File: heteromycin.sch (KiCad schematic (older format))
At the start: 0 parts

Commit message: Current snapshot
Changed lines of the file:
@@
 $Descr A4 11693 8268
 encoding utf-8
-Sheet 1 7
+Sheet 1 11
 Title ""
 Date ""
@@
 $EndSheet
 $Sheet
-S 8550 1950 1600 950
+S 8550 1950 1600 600
 U 5BC2F52C
 F0 "Stepper Motor X" 50
@@
 F1 "mosfets.sch" 50
 $EndSheet
+$Sheet
+S 8550 2750 1600 600
+U 5BC77BE8
+F0 "Steper Motor Y" 50
+F1 "motor.sch" 50
+$EndSheet
+$Sheet
+S 8550 3550 1600 600
+U 5BC77F87
+F0 "Stepper Motor Z" 50
+F1 "motor.sch" 50
+$EndSheet
+$Sheet
+S 8550 4350 1600 600
+U 5BC77F8A
+F0 "Stepper Motor E0" 50
+F1 "motor.sch" 50
+$EndSheet
+$Sheet
+S 8550 5150 1600 600
+U 5BC77F8D
+F0 "Stepper Motor E1" 50
+F1 "motor.sch" 50
+$EndSheet
 $EndSCHEMATC

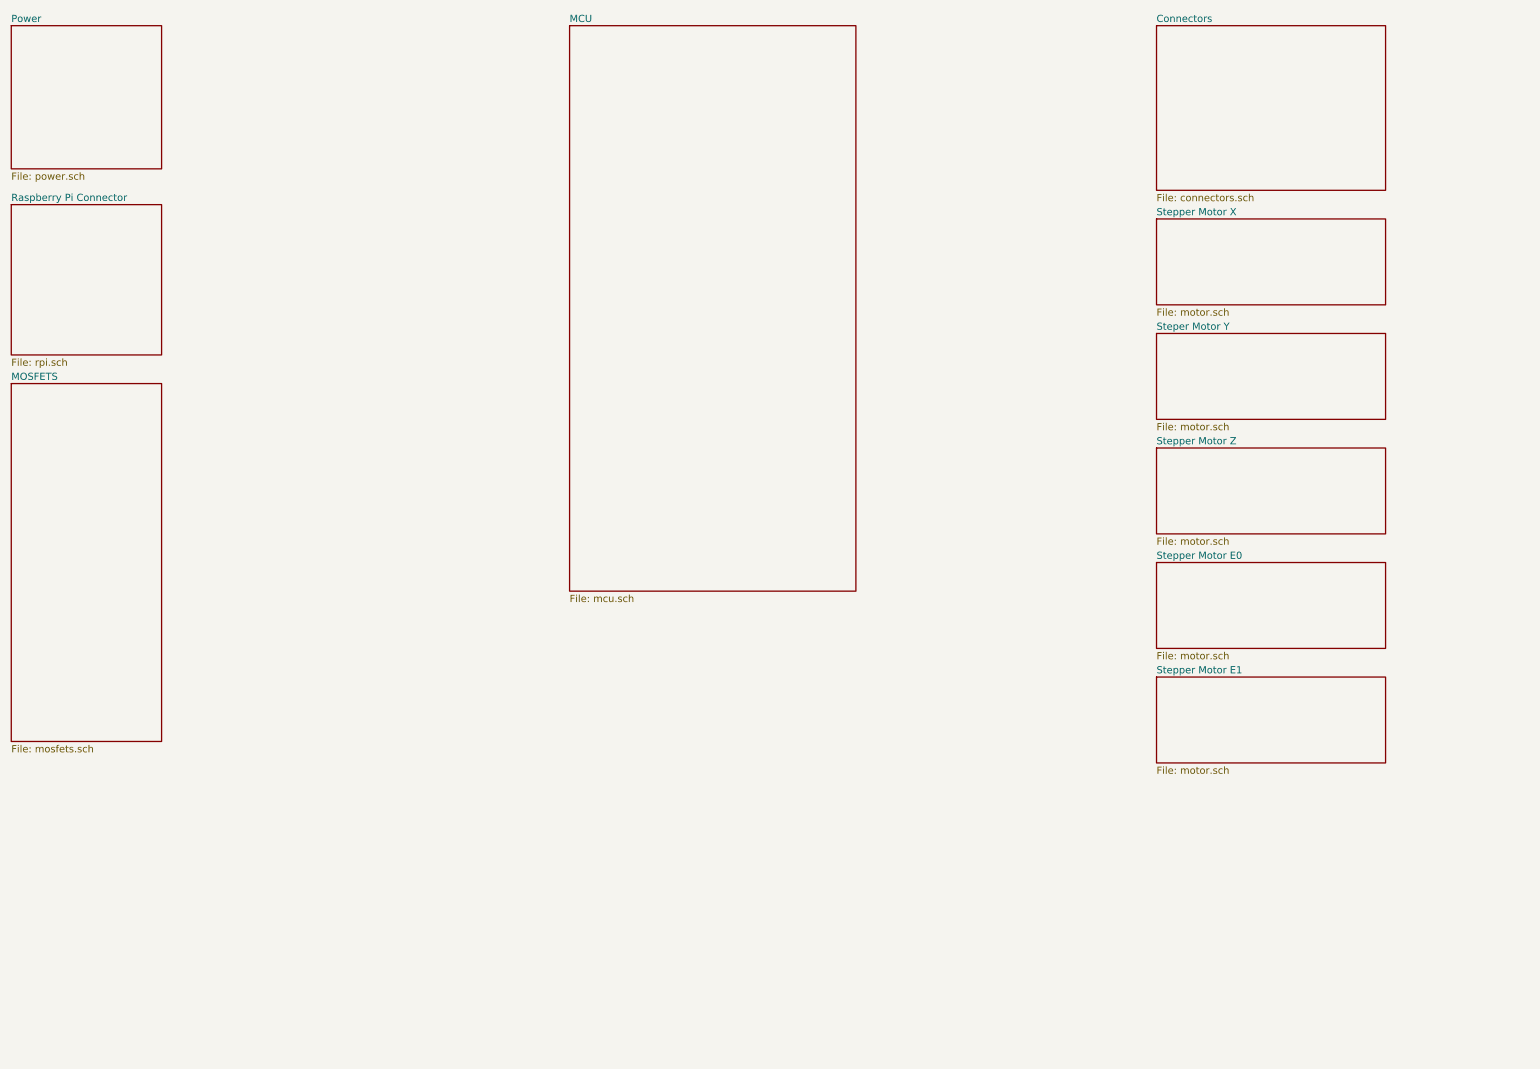
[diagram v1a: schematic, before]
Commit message: Add SD card reader, placed temp connections, fixed stepper placement
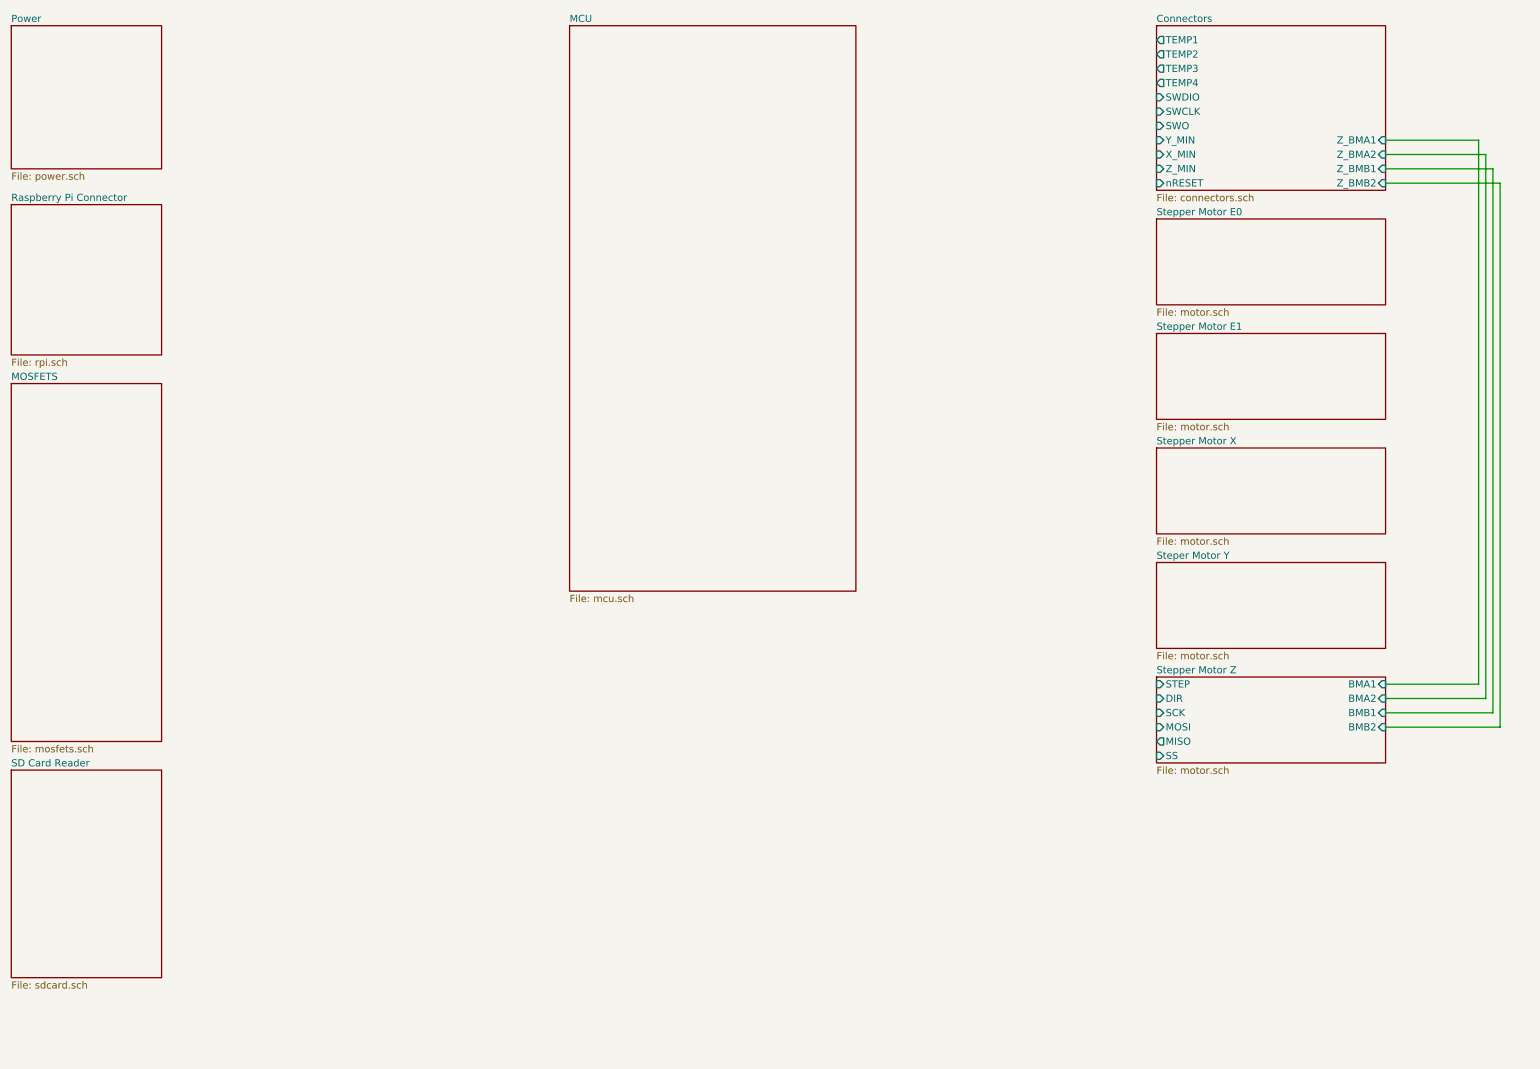
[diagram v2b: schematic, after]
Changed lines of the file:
@@
 $Descr A4 11693 8268
 encoding utf-8
-Sheet 1 11
+Sheet 1 12
 Title ""
 Date ""
@@
 F0 "Connectors" 50
 F1 "connectors.sch" 50
+F2 "TEMP1" O L 8550 700 50
+F3 "TEMP2" O L 8550 800 50
+F4 "TEMP3" O L 8550 900 50
+F5 "nRESET" I L 8550 1700 50
+F6 "SWDIO" I L 8550 1100 50
+F7 "SWCLK" I L 8550 1200 50
+F8 "Z_MIN" I L 8550 1600 50
+F9 "Y_MIN" I L 8550 1400 50
+F10 "Z_BMB1" I R 10150 1600 50
+F11 "Z_BMB2" I R 10150 1700 50
+F12 "Z_BMA2" I R 10150 1500 50
+F13 "Z_BMA1" I R 10150 1400 50
+F14 "X_MIN" I L 8550 1500 50
+F15 "SWO" I L 8550 1300 50
+F16 "TEMP4" O L 8550 1000 50
 $EndSheet
 $Sheet
-S 8550 1950 1600 600
+S 8550 3550 1600 600
 U 5BC2F52C
 F0 "Stepper Motor X" 50
@@
 $EndSheet
 $Sheet
-S 8550 2750 1600 600
+S 8550 4350 1600 600
 U 5BC77BE8
 F0 "Steper Motor Y" 50
@@
 $EndSheet
 $Sheet
-S 8550 3550 1600 600
+S 8550 5150 1600 600
 U 5BC77F87
 F0 "Stepper Motor Z" 50
 F1 "motor.sch" 50
+F2 "STEP" I L 8550 5200 50
+F3 "DIR" I L 8550 5300 50
+F4 "SCK" I L 8550 5400 50
+F5 "MOSI" I L 8550 5500 50
+F6 "MISO" O L 8550 5600 50
+F7 "BMA1" I R 10150 5200 50
+F8 "BMA2" I R 10150 5300 50
+F9 "BMB2" I R 10150 5500 50
+F10 "BMB1" I R 10150 5400 50
+F11 "SS" I L 8550 5700 50
 $EndSheet
 $Sheet
-S 8550 4350 1600 600
+S 8550 1950 1600 600
 U 5BC77F8A
 F0 "Stepper Motor E0" 50
@@
 $EndSheet
 $Sheet
-S 8550 5150 1600 600
+S 8550 2750 1600 600
 U 5BC77F8D
 F0 "Stepper Motor E1" 50
 F1 "motor.sch" 50
 $EndSheet
+Wire Wire Line
+	10150 5200 10800 5200
+Wire Wire Line
+	10800 5200 10800 1400
+Wire Wire Line
+	10800 1400 10150 1400
+Wire Wire Line
+	10150 1500 10850 1500
+Wire Wire Line
+	10850 1500 10850 5300
+Wire Wire Line
+	10850 5300 10150 5300
+Wire Wire Line
+	10150 5400 10900 5400
+Wire Wire Line
+	10900 5400 10900 1600
+Wire Wire Line
+	10900 1600 10150 1600
+Wire Wire Line
+	10150 1700 10950 1700
+Wire Wire Line
+	10950 1700 10950 5500
+Wire Wire Line
+	10950 5500 10150 5500
+$Sheet
+S 550  5800 1050 1450
+U 5BC78E83
+F0 "SD Card Reader" 50
+F1 "sdcard.sch" 50
+$EndSheet
 $EndSCHEMATC

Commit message: Some small adjustments
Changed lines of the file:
@@
 $EndDescr
 $Sheet
-S 550  1850 1050 1050
+S 550  600  1050 1050
 U 5BC4AC32
 F0 "Raspberry Pi Connector" 50
@@
 $EndSheet
 $Sheet
-S 550  600  1050 1000
+S 5700 6550 1150 1100
 U 5BC54251
 F0 "Power" 50
@@
 $EndSheet
 $Sheet
-S 4450 600  2000 3950
+S 4350 600  2000 3950
 U 5BC1C8A4
 F0 "MCU" 50
@@
 $EndSheet
 $Sheet
-S 8550 600  1600 1150
+S 550  4300 1050 650
+U 5BC2F52C
+F0 "Stepper Motor X" 50
+F1 "motor.sch" 50
+F2 "STEP" I R 1600 4350 50
+F3 "DIR" I R 1600 4450 50
+F4 "SCK" I R 1600 4550 50
+F5 "MOSI" I R 1600 4650 50
+F6 "MISO" O R 1600 4750 50
+F7 "SS" I R 1600 4850 50
+$EndSheet
+$Sheet
+S 550  1800 1050 750
+U 5BC2F648
+F0 "MOSFETS" 50
+F1 "mosfets.sch" 50
+F2 "PWM_BED" I R 1600 1850 50
+F3 "PWM_HEAT1" I R 1600 1950 50
+F4 "PWM_FAN1" I R 1600 2150 50
+F5 "PWM_FAN3" I R 1600 2350 50
+F6 "PWM_HEAT2" I R 1600 2050 50
+F7 "PWM_FAN2" I R 1600 2250 50
+F8 "PWM_FAN4" I R 1600 2450 50
+$EndSheet
+$Sheet
+S 550  5100 1050 650
+U 5BC77BE8
+F0 "Steper Motor Y" 50
+F1 "motor.sch" 50
+F2 "STEP" I R 1600 5150 50
+F3 "DIR" I R 1600 5250 50
+F4 "SCK" I R 1600 5350 50
+F5 "MOSI" I R 1600 5450 50
+F6 "MISO" O R 1600 5550 50
+F7 "SS" I R 1600 5650 50
+$EndSheet
+$Sheet
+S 550  5900 1050 1050
+U 5BC77F87
+F0 "Stepper Motor Z" 50
+F1 "motor.sch" 50
+F2 "STEP" I R 1600 5950 50
+F3 "DIR" I R 1600 6050 50
+F4 "SCK" I R 1600 6150 50
+F5 "MOSI" I R 1600 6250 50
+F6 "MISO" O R 1600 6350 50
+F7 "BMA1" I R 1600 6550 50
+F8 "BMA2" I R 1600 6650 50
+F9 "BMB2" I R 1600 6850 50
+F10 "BMB1" I R 1600 6750 50
+F11 "SS" I R 1600 6450 50
+$EndSheet
+$Sheet
+S 550  3500 1050 650
+U 5BC77F8A
+F0 "Stepper Motor E0" 50
+F1 "motor.sch" 50
+F2 "STEP" I R 1600 3550 50
+F3 "DIR" I R 1600 3650 50
+F4 "SCK" I R 1600 3750 50
+F5 "MOSI" I R 1600 3850 50
+F6 "MISO" O R 1600 3950 50
+F7 "SS" I R 1600 4050 50
+$EndSheet
+$Sheet
+S 550  2700 1050 650
+U 5BC77F8D
+F0 "Stepper Motor E1" 50
+F1 "motor.sch" 50
+F2 "STEP" I R 1600 2750 50
+F3 "DIR" I R 1600 2850 50
+F4 "SCK" I R 1600 2950 50
+F5 "MOSI" I R 1600 3050 50
+F6 "MISO" O R 1600 3150 50
+F7 "SS" I R 1600 3250 50
+$EndSheet
+$Sheet
+S 9800 600  1350 550
+U 5BC78E83
+F0 "SD Card Reader" 50
+F1 "sdcard.sch" 50
+F2 "MISO" I L 9800 850 50
+F3 "MOSI" I L 9800 750 50
+F4 "SCK" I L 9800 650 50
+F5 "SD_DETECT" I L 9800 1050 50
+F6 "SS" I L 9800 950 50
+$EndSheet
+$Sheet
+S 9800 1300 1350 4100
 U 5BC2F290
 F0 "Connectors" 50
 F1 "connectors.sch" 50
-F2 "TEMP1" O L 8550 700 50
-F3 "TEMP2" O L 8550 800 50
-F4 "TEMP3" O L 8550 900 50
-F5 "nRESET" I L 8550 1700 50
-F6 "SWDIO" I L 8550 1100 50
-F7 "SWCLK" I L 8550 1200 50
-F8 "Z_MIN" I L 8550 1600 50
-F9 "Y_MIN" I L 8550 1400 50
-F10 "Z_BMB1" I R 10150 1600 50
-F11 "Z_BMB2" I R 10150 1700 50
-F12 "Z_BMA2" I R 10150 1500 50
-F13 "Z_BMA1" I R 10150 1400 50
-F14 "X_MIN" I L 8550 1500 50
-F15 "SWO" I L 8550 1300 50
-F16 "TEMP4" O L 8550 1000 50
-$EndSheet
-$Sheet
-S 8550 3550 1600 600
-U 5BC2F52C
-F0 "Stepper Motor X" 50
-F1 "motor.sch" 50
-$EndSheet
-$Sheet
-S 550  3100 1050 2500
-U 5BC2F648
-F0 "MOSFETS" 50
-F1 "mosfets.sch" 50
-$EndSheet
-$Sheet
-S 8550 4350 1600 600
-U 5BC77BE8
-F0 "Steper Motor Y" 50
-F1 "motor.sch" 50
-$EndSheet
-$Sheet
-S 8550 5150 1600 600
-U 5BC77F87
-F0 "Stepper Motor Z" 50
-F1 "motor.sch" 50
-F2 "STEP" I L 8550 5200 50
-F3 "DIR" I L 8550 5300 50
-F4 "SCK" I L 8550 5400 50
-F5 "MOSI" I L 8550 5500 50
-F6 "MISO" O L 8550 5600 50
-F7 "BMA1" I R 10150 5200 50
-F8 "BMA2" I R 10150 5300 50
-F9 "BMB2" I R 10150 5500 50
-F10 "BMB1" I R 10150 5400 50
-F11 "SS" I L 8550 5700 50
-$EndSheet
-$Sheet
-S 8550 1950 1600 600
-U 5BC77F8A
-F0 "Stepper Motor E0" 50
-F1 "motor.sch" 50
-$EndSheet
-$Sheet
-S 8550 2750 1600 600
-U 5BC77F8D
-F0 "Stepper Motor E1" 50
-F1 "motor.sch" 50
+F2 "Z_BMB1" I L 9800 5250 50
+F3 "Z_BMB2" I L 9800 5350 50
+F4 "Z_BMA2" I L 9800 5150 50
+F5 "Z_BMA1" I L 9800 5050 50
+F6 "TEMP1" O L 9800 2550 50
+F7 "TEMP2" O L 9800 2650 50
+F8 "TEMP3" O L 9800 2850 50
+F9 "nRESET" I L 9800 3450 50
+F10 "SWDIO" I L 9800 3250 50
+F11 "SWCLK" I L 9800 3150 50
+F12 "Z_MIN" I L 9800 4000 50
+F13 "Y_MIN" I L 9800 3900 50
+F14 "X_MIN" I L 9800 3800 50
+F15 "SWO" I L 9800 3350 50
+F16 "TEMP4" O L 9800 2750 50
 $EndSheet
 Wire Wire Line
-	10150 5200 10800 5200
+	1600 6850 5550 6850
 Wire Wire Line
-	10800 5200 10800 1400
+	5550 6850 5550 6400
 Wire Wire Line
-	10800 1400 10150 1400
+	5550 6400 9600 6400
 Wire Wire Line
-	10150 1500 10850 1500
+	9600 6400 9600 5350
 Wire Wire Line
-	10850 1500 10850 5300
+	9600 5350 9800 5350
 Wire Wire Line
-	10850 5300 10150 5300
+	9800 5250 9500 5250
 Wire Wire Line
-	10150 5400 10900 5400
+	9500 5250 9500 6300
 Wire Wire Line
-	10900 5400 10900 1600
+	9500 6300 5450 6300
 Wire Wire Line
-	10900 1600 10150 1600
+	5450 6300 5450 6750
 Wire Wire Line
-	10150 1700 10950 1700
+	5450 6750 1600 6750
 Wire Wire Line
-	10950 1700 10950 5500
+	1600 6650 5350 6650
 Wire Wire Line
-	10950 5500 10150 5500
-$Sheet
-S 550  5800 1050 1450
-U 5BC78E83
-F0 "SD Card Reader" 50
-F1 "sdcard.sch" 50
-$EndSheet
+	5350 6650 5350 6200
+Wire Wire Line
+	5350 6200 9400 6200
+Wire Wire Line
+	9400 6200 9400 5150
+Wire Wire Line
+	9400 5150 9800 5150
+Wire Wire Line
+	9800 5050 9300 5050
+Wire Wire Line
+	9300 5050 9300 6100
+Wire Wire Line
+	9300 6100 5250 6100
+Wire Wire Line
+	5250 6100 5250 6550
+Wire Wire Line
+	5250 6550 1600 6550
 $EndSCHEMATC

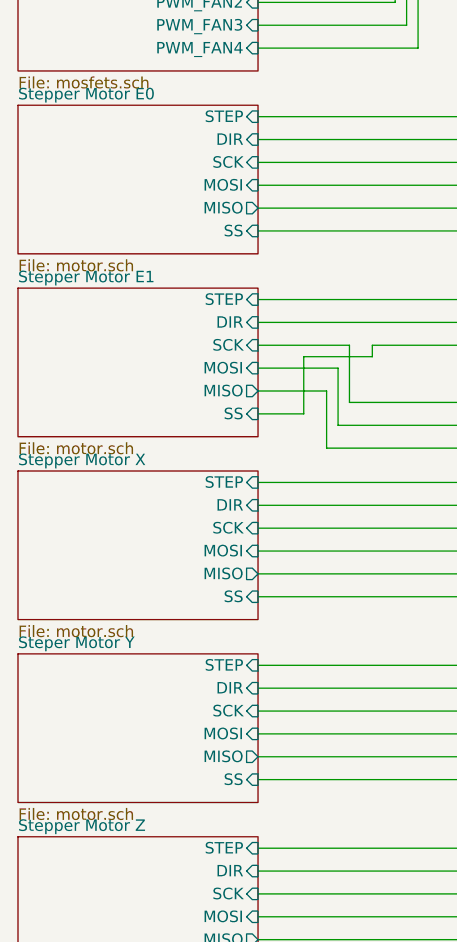
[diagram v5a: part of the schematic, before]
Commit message: Finish silkscreen and updated README.md
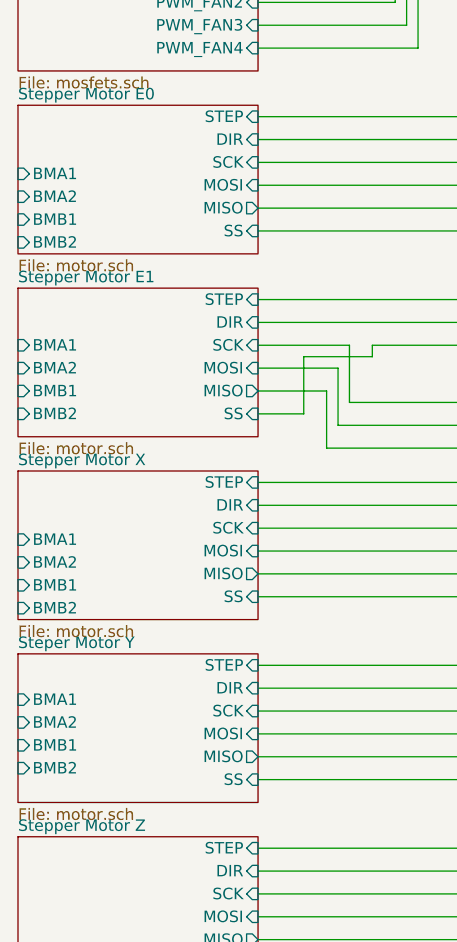
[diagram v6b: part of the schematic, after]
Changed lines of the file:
@@
 F6 "MISO" O R 1600 5500 50
 F7 "SS" I R 1600 5600 50
+F8 "BMA2" I L 550 5450 50
+F9 "BMA1" I L 550 5350 50
+F10 "BMB2" I L 550 5650 50
+F11 "BMB1" I L 550 5550 50
 $EndSheet
 $Sheet
@@
 F6 "MISO" O R 1600 6300 50
 F7 "SS" I R 1600 6400 50
+F8 "BMA2" I L 550 6150 50
+F9 "BMA1" I L 550 6050 50
+F10 "BMB2" I L 550 6350 50
+F11 "BMB1" I L 550 6250 50
 $EndSheet
 $Sheet
@@
 F6 "MISO" O R 1600 3900 50
 F7 "SS" I R 1600 4000 50
+F8 "BMA2" I L 550 3850 50
+F9 "BMA1" I L 550 3750 50
+F10 "BMB2" I L 550 4050 50
+F11 "BMB1" I L 550 3950 50
 $EndSheet
 $Sheet
@@
 F6 "MISO" O R 1600 4700 50
 F7 "SS" I R 1600 4800 50
+F8 "BMA2" I L 550 4600 50
+F9 "BMA1" I L 550 4500 50
+F10 "BMB2" I L 550 4800 50
+F11 "BMB1" I L 550 4700 50
 $EndSheet
 $Sheet
